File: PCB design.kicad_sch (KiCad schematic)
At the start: 1 part

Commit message: hello
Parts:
- added Male_Connector: TFM-105-02-L-D-WT, TFM-105-02-XXX-D-WT, symbol TFM-105-02-L-D-WT:TFM-105-02-L-D-WT
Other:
- note added: "Female connector"
- note added: "Male connector"
- moved on the sheet: Female_Connector

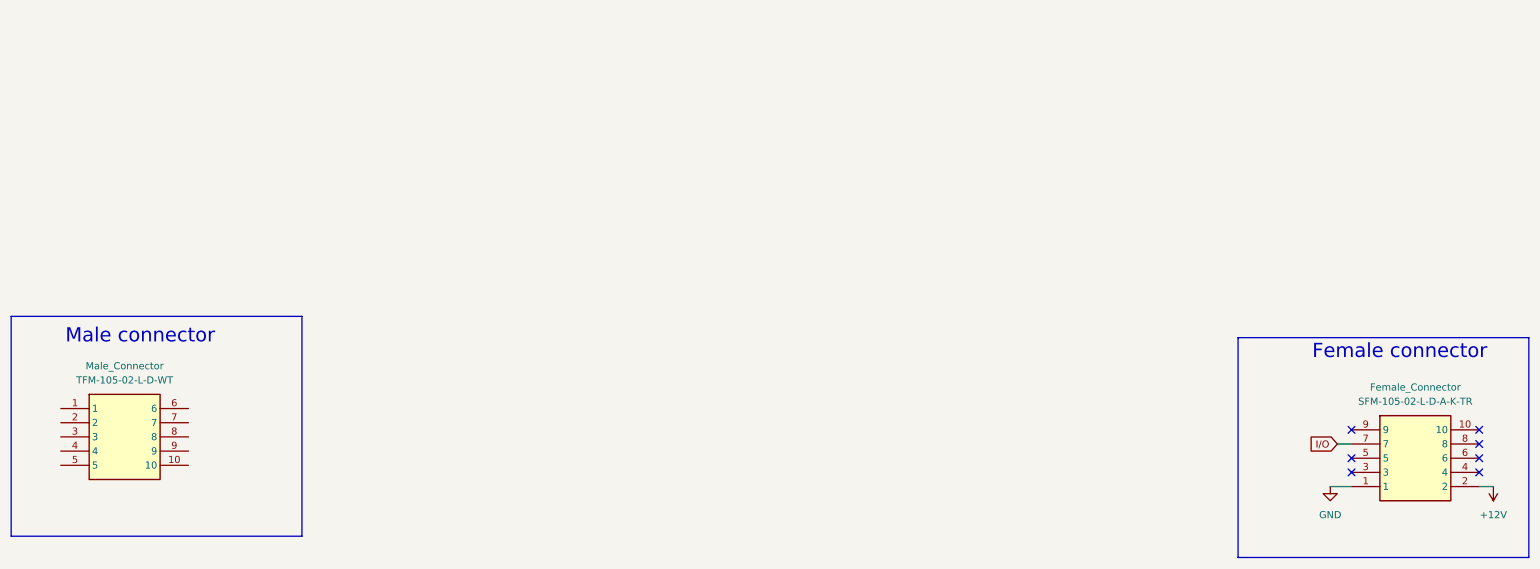
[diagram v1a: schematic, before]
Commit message: Added a fixed power regulator symbol for 12V and fixed the male pin head
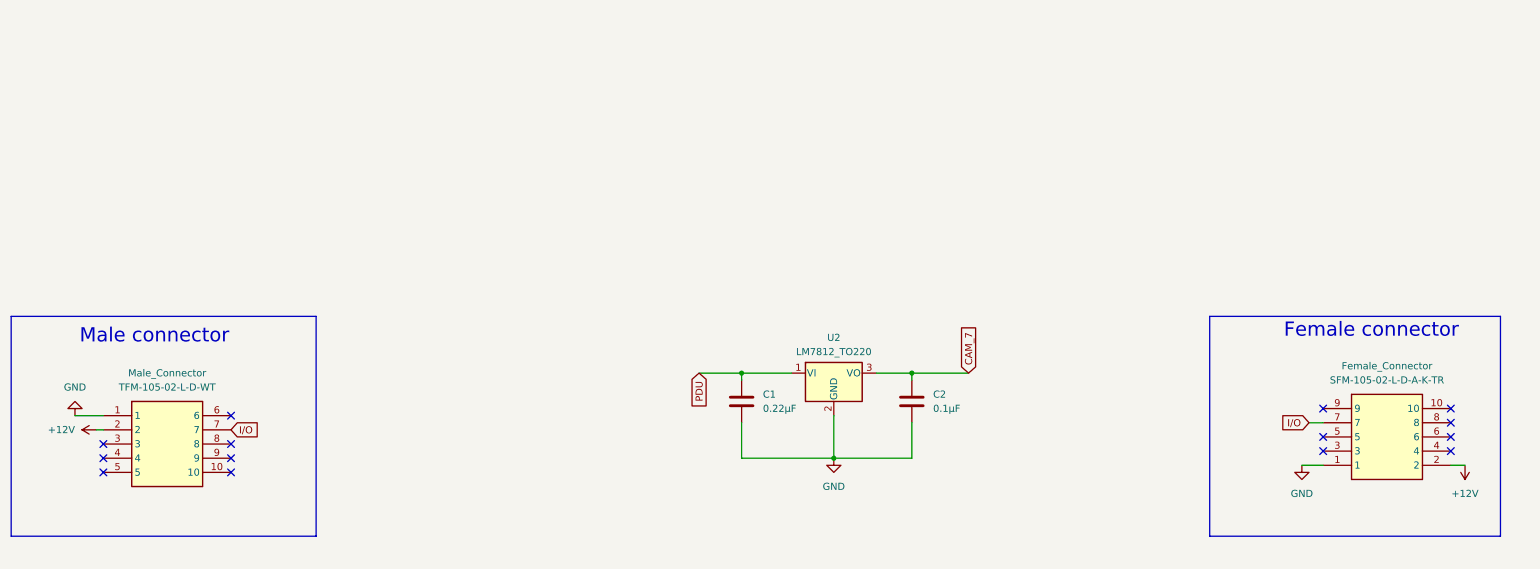
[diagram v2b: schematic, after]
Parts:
- added C1: 0.22µF, symbol Device:C
- added C2: 0.1µF, symbol Device:C
- added U2: LM7812_TO220, Package_TO_SOT_THT:TO-220-3_Vertical, symbol Regulator_Linear:LM7812_TO220
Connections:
- net +12V: now also Male_Connector.2
- net GND: now also Male_Connector.1, C1.2, C2.2, U2.2 (GND)
- net I/O: now also Male_Connector.7
- new net CAM_7: C2.1, U2.3 (VO)
- new net PDU: C1.1, U2.1 (VI)
- no-connect marks 7 -> 14
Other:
- moved on the sheet: Female_Connector, Male_Connector

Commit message: Added a sphynx diode and proper capasitors and grounded and labeled their respective ports git push origin main oh sorry i think im still writing the message
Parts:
- added D3: D_Schottky, Diode_SMD:D_0603_1608Metric, symbol Device:D_Schottky
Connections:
- net CAM_7 is gone; now on net +12V: C2.1, U2.3 (VO)
- net +12V: no longer Male_Connector.2
- net PDU: now also Male_Connector.2, D3.2 (A); no longer U2.1 (VI)
- new net: D3.1 (K), U2.1 (VI)
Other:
- moved on the sheet: C1, C2, U2

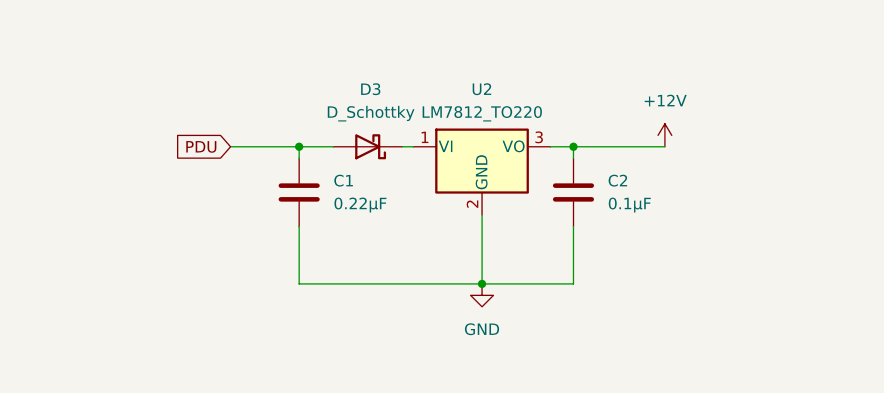
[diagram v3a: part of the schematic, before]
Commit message: Boxed the PWR regulator and gave it a it a title
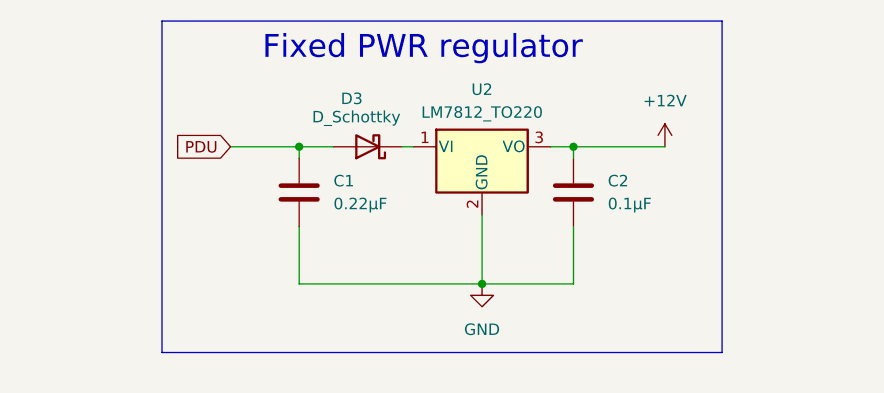
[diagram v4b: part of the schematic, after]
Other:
- note added: "Fixed PWR regulator"
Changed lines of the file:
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@@
+		)
+	)
+	(rectangle
+		(start 127 74.93)
+		(end 189.23 111.76)
+		(stroke
+			(width 0)
+			(type default)
+		)
+		(fill
+			(type none)
+		)
+	)
+	(text "Fixed PWR regulator\n"
+		(exclude_from_sim no)
+		(at 155.956 77.978 0)
+		(effects
+			(font
+				(size 2.54 2.54)
+			)
 		)
 	)
@@
 		(in_pos_files yes)
 		(dnp no)
-		(fields_autoplaced yes)
 		(property "Reference" "D3"
-			(at 150.1775 82.55 0)
+			(at 148.082 83.566 0)
 			(show_name no)
 			(do_not_autoplace no)
@@
 		)
 		(property "Value" "D_Schottky"
-			(at 150.1775 85.09 0)
-			(show_name no)
-			(do_not_autoplace no)
+			(at 148.59 85.598 0)
+			(show_name no)
+			(do_not_autoplace no)
